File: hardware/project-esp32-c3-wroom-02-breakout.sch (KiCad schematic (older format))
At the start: 10 parts, among them IC1 ESP32-WROVER-E_M213EH6464PH3Q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, J1 Conn_01x06_Male, J2 Conn_01x10_Male, J3 Conn_01x10_Male, Q1 MUN5214DW1T1G, U1 XC6220B331MR

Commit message: Schematic ready
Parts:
- removed C3: 0.1uF, Capacitor_SMD:C_0603_1608Metric_Pad1.08x0.95mm_HandSolder, symbol Device:C_Small
- removed IC1: ESP32-WROVER-E_M213EH6464PH3Q0_, ESP32WROVEREM213EH6464PH3Q0, symbol ESP32-WROVER-E_M213EH6464PH3Q0:ESP32-WROVER-E_M213EH6464PH3Q0_
- removed J1: Conn_01x06_Male, B6B-ZR(LF)(SN):JST_B6B-ZR(LF)(SN), symbol Connector:Conn_01x06_Male
- removed J2, J3: Conn_01x10_Male, Connector_PinHeader_2.54mm:PinHeader_1x10_P2.54mm_Vertical, symbol Connector:Conn_01x10_Male
- removed R1: 10k, Resistor_SMD:R_0603_1608Metric_Pad0.98x0.95mm_HandSolder, symbol Device:R_Small
- added C? (x2): 0.1uF, Capacitor_SMD:C_0603_1608Metric_Pad1.08x0.95mm_HandSolder, symbol Device:C_Small
- added C? (x2): 22pF, Capacitor_SMD:C_0603_1608Metric_Pad1.08x0.95mm_HandSolder, symbol Device:C_Small
- added J?: SM04B-SRSS-TB(LF)(SN), JST_SM04B-SRSS-TB(LF)(SN), symbol SM04B-SRSS-TB_LF__SN_:SM04B-SRSS-TB(LF)(SN)
- added J? (x2): Conn_01x08_Male, symbol Connector:Conn_01x08_Male
- added JP?: SolderJumper_3_Bridged12, symbol Jumper:SolderJumper_3_Bridged12
- added R? (x3): 10k, Resistor_SMD:R_0603_1608Metric_Pad0.98x0.95mm_HandSolder, symbol Device:R_Small
- added R? (x2): 4k7, Resistor_SMD:R_0603_1608Metric_Pad0.98x0.95mm_HandSolder, symbol Device:R_Small
- added U?: ESP32-C3-WROOM-02-H4, MODULE_ESP32-C3-WROOM-02-H4, symbol ESP32-C3-WROOM-02-H4:ESP32-C3-WROOM-02-H4
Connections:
- net labels added: 3V3, GPIO1, GPIO10, GPIO3, GPIO6, GPIO7, GPIO8, GPIO9, SCL, SDA, USB_D+, USB_D-, VCC
- net labels removed: +5V, GPIO14, GPIO15, GPIO18, GPIO19, GPIO21, GPIO22, GPIO23, GPIO25, GPIO26, GPIO27, GPIO32, GPIO33
- wire segments 111 -> 106
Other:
- note added: "Auto Download Boot"
- note added: "Boot Strapping Pins"
- note added: "Connectors"
- note added: "ESP32 Module"
- note added: "I2C/StemmaQT"
- note added: "Regulator"
- note added: "USB"
- note added: "←"
- moved on the sheet: Q1A, Q1B

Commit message: First placement done
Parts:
- added D1: LED, LED_SMD:LED_0603_1608Metric, symbol Device:LED
- added R6: 10k, Resistor_SMD:R_0603_1608Metric_Pad0.98x0.95mm_HandSolder, symbol Device:R_Small
- J2, J3: renamed from J?; footprint (none) -> Connector_PinHeader_2.54mm:PinHeader_1x08_P2.54mm_Vertical
- JP1: renamed from JP?; footprint (none) -> Jumper:SolderJumper-3_P1.3mm_Bridged12_RoundedPad1.0x1.5mm
- gave numbers to parts that had none: 11
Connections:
- wire segments 106 -> 109
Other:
- note added: "Power LED"
- moved on the sheet: J3

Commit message: Routing done
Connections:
- net labels removed: SCL, SDA
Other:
- note added: "(SCL)"
- note added: "(SDA)"
- moved on the sheet: J1, JP1
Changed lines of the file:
@@
 	2800 1400 2800 1300
 Connection ~ 2800 1400
+Text Label 10150 5400 0    50   ~ 0
+RX
 Text Label 10150 5300 0    50   ~ 0
-RX
-Text Label 10150 5400 0    50   ~ 0
 TX
 Text Label 2550 5150 0    50   ~ 0
@@
 Wire Wire Line
 	2550 5850 2850 5850
-Text Label 4300 5350 0    50   ~ 0
-USB_D+
-Text Label 4300 5450 0    50   ~ 0
-USB_D-
-Text Label 4650 5350 0    50   ~ 0
-SDA
-Text Label 4650 5450 0    50   ~ 0
-SCL
-Wire Wire Line
-	4800 5350 4250 5350
-Wire Wire Line
-	4800 5450 4250 5450
 $Comp
 L power:VCC #PWR0108
@@
 Wire Wire Line
 	4900 4400 4900 4350
-Text Label 7450 3100 0    50   ~ 0
-USB_D+
-Text Label 7450 3200 0    50   ~ 0
-USB_D-
-Text Label 9750 3650 0    50   ~ 0
-SDA
-Text Label 9750 3750 0    50   ~ 0
-SCL
 $Comp
 L Device:C_Small C5
@@
 $EndComp
 Wire Wire Line
-	9750 3650 10100 3650
-Wire Wire Line
 	10100 3650 10100 3500
 Wire Wire Line
 	10100 3300 10100 3250
-Wire Wire Line
-	9750 3750 10400 3750
 Wire Wire Line
 	10400 3750 10400 3500
@@
 	9350 5500 9650 5500
 Wire Wire Line
+	10150 5400 10450 5400
+Wire Wire Line
 	10150 5300 10450 5300
-Wire Wire Line
-	10150 5400 10450 5400
 Wire Wire Line
 	10150 5500 10450 5500
@@
 Wire Wire Line
 	9350 5000 9650 5000
-Text Notes 7600 5100 0    197  ~ 0
+Text Notes 7800 5100 0    197  ~ 0
 ←
-Text Notes 8000 5100 0    197  ~ 0
+Text Notes 8200 5100 0    197  ~ 0
 ←
 Wire Wire Line
-	8150 4900 8150 4800
-Wire Wire Line
-	8100 4900 8150 4900
+	8350 4900 8350 4800
+Wire Wire Line
+	8300 4900 8350 4900
 $Comp
 L power:+3.3V #PWR0113
 U 1 1 617D3310
-P 8150 4800
-F 0 "#PWR0113" H 8150 4650 50  0001 C CNN
-F 1 "+3.3V" H 8165 4973 50  0000 C CNN
-F 2 "" H 8150 4800 50  0001 C CNN
-F 3 "" H 8150 4800 50  0001 C CNN
-	1    8150 4800
-	1    0    0    -1
-$EndComp
-Wire Wire Line
-	7650 4900 7700 4900
-Wire Wire Line
-	7650 4800 7650 4900
+P 8350 4800
+F 0 "#PWR0113" H 8350 4650 50  0001 C CNN
+F 1 "+3.3V" H 8365 4973 50  0000 C CNN
+F 2 "" H 8350 4800 50  0001 C CNN
+F 3 "" H 8350 4800 50  0001 C CNN
+	1    8350 4800
+	1    0    0    -1
+$EndComp
+Wire Wire Line
+	7850 4900 7900 4900
+Wire Wire Line
+	7850 4800 7850 4900
 $Comp
 L power:VCC #PWR0114
 U 1 1 617CC8C4
-P 7650 4800
-F 0 "#PWR0114" H 7650 4650 50  0001 C CNN
-F 1 "VCC" H 7665 4973 50  0000 C CNN
-F 2 "" H 7650 4800 50  0001 C CNN
-F 3 "" H 7650 4800 50  0001 C CNN
-	1    7650 4800
-	1    0    0    -1
-$EndComp
-Wire Wire Line
-	7900 5050 7900 5300
+P 7850 4800
+F 0 "#PWR0114" H 7850 4650 50  0001 C CNN
+F 1 "VCC" H 7865 4973 50  0000 C CNN
+F 2 "" H 7850 4800 50  0001 C CNN
+F 3 "" H 7850 4800 50  0001 C CNN
+	1    7850 4800
+	1    0    0    -1
+$EndComp
+Wire Wire Line
+	8100 5050 8100 5300
 $Comp
 L Jumper:SolderJumper_3_Bridged12 JP1
 U 1 1 617A1A5E
-P 7900 4900
-F 0 "JP1" H 7900 5013 50  0000 C CNN
-F 1 "SolderJumper_3_Bridged12" H 7900 5014 50  0001 C CNN
-F 2 "Jumper:SolderJumper-3_P1.3mm_Bridged12_RoundedPad1.0x1.5mm" H 7900 4900 50  0001 C CNN
-F 3 "~" H 7900 4900 50  0001 C CNN
-	1    7900 4900
-	1    0    0    -1
-$EndComp
-Wire Wire Line
-	7700 5700 7700 5200
-Connection ~ 7700 5700
-Wire Wire Line
-	8000 5700 7700 5700
-Wire Wire Line
-	7800 5500 8000 5500
-Wire Wire Line
-	8000 5400 7800 5400
-Text Label 7800 5400 0    50   ~ 0
-SDA
-Text Label 7800 5500 0    50   ~ 0
-SCL
+P 8100 4900
+F 0 "JP1" H 8100 5013 50  0000 C CNN
+F 1 "SolderJumper_3_Bridged12" H 8100 5014 50  0001 C CNN
+F 2 "Jumper:SolderJumper-3_P1.3mm_Bridged12_RoundedPad1.0x1.5mm" H 8100 4900 50  0001 C CNN
+F 3 "~" H 8100 4900 50  0001 C CNN
+	1    8100 4900
+	1    0    0    -1
+$EndComp
+Wire Wire Line
+	8200 5700 7550 5700
 $Comp
 L power:GND #PWR0115
 U 1 1 616AF751
-P 7700 5800
-F 0 "#PWR0115" H 7700 5550 50  0001 C CNN
-F 1 "GND" H 7705 5627 50  0000 C CNN
-F 2 "" H 7700 5800 50  0001 C CNN
-F 3 "" H 7700 5800 50  0001 C CNN
-	1    7700 5800
-	1    0    0    -1
-$EndComp
-Wire Wire Line
-	7700 5800 7700 5700
-Wire Wire Line
-	7700 5200 8000 5200
-Wire Wire Line
-	7900 5300 8000 5300
+P 7550 5800
+F 0 "#PWR0115" H 7550 5550 50  0001 C CNN
+F 1 "GND" H 7555 5627 50  0000 C CNN
+F 2 "" H 7550 5800 50  0001 C CNN
+F 3 "" H 7550 5800 50  0001 C CNN
+	1    7550 5800
+	1    0    0    -1
+$EndComp
+Wire Wire Line
+	7550 5800 7550 5700
+Wire Wire Line
+	8100 5300 8200 5300
 $Comp
 L SM04B-SRSS-TB_LF__SN_:SM04B-SRSS-TB(LF)(SN) J1
 U 1 1 6168E703
-P 8300 5400
-F 0 "J1" H 8530 5350 50  0000 L CNN
-F 1 "SM04B-SRSS-TB(LF)(SN)" H 8530 5305 50  0001 L CNN
-F 2 "JST_SM04B-SRSS-TB(LF)(SN)" H 8300 5400 50  0001 L BNN
-F 3 "" H 8300 5400 50  0001 L BNN
-F 4 "Manufacturer recommendations" H 8300 5400 50  0001 L BNN "STANDARD"
-F 5 "JST" H 8300 5400 50  0001 L BNN "MANUFACTURER"
-	1    8300 5400
+P 8500 5400
+F 0 "J1" H 8730 5350 50  0000 L CNN
+F 1 "SM04B-SRSS-TB(LF)(SN)" H 8730 5305 50  0001 L CNN
+F 2 "JST_SM04B-SRSS-TB(LF)(SN)" H 8500 5400 50  0001 L BNN
+F 3 "" H 8500 5400 50  0001 L BNN
+F 4 "Manufacturer recommendations" H 8500 5400 50  0001 L BNN "STANDARD"
+F 5 "JST" H 8500 5400 50  0001 L BNN "MANUFACTURER"
+	1    8500 5400
 	1    0    0    -1
 $EndComp
@@
 Text Notes 8850 650  0    50   ~ 0
 Power LED
+Text Label 9550 3750 0    50   ~ 0
+USB_D+
+Text Label 9550 3650 0    50   ~ 0
+USB_D-
+Wire Wire Line
+	9550 3650 10100 3650
+Wire Wire Line
+	9550 3750 10400 3750
+Text Label 7450 3200 0    50   ~ 0
+USB_D+
+Text Label 7450 3100 0    50   ~ 0
+USB_D-
+Text Label 7900 5400 0    50   ~ 0
+USB_D+
+Text Label 7900 5500 0    50   ~ 0
+USB_D-
+Wire Wire Line
+	7550 5200 7550 5700
+Wire Wire Line
+	7550 5200 8200 5200
+Connection ~ 7550 5700
+Text Label 4300 5450 0    50   ~ 0
+USB_D+
+Wire Wire Line
+	4550 5350 4250 5350
+Wire Wire Line
+	4550 5450 4250 5450
+Text Notes 9300 3750 0    50   ~ 0
+(SDA)
+Text Notes 9300 3650 0    50   ~ 0
+(SCL)
+Text Notes 7650 5400 0    50   ~ 0
+(SDA)
+Text Notes 7650 5500 0    50   ~ 0
+(SCL)
+Wire Wire Line
+	7900 5400 8200 5400
+Wire Wire Line
+	7900 5500 8200 5500
+Text Label 4300 5350 0    50   ~ 0
+USB_D-
+Text Notes 4650 5450 0    50   ~ 0
+(SDA)
+Text Notes 4650 5350 0    50   ~ 0
+(SCL)
 $EndSCHEMATC

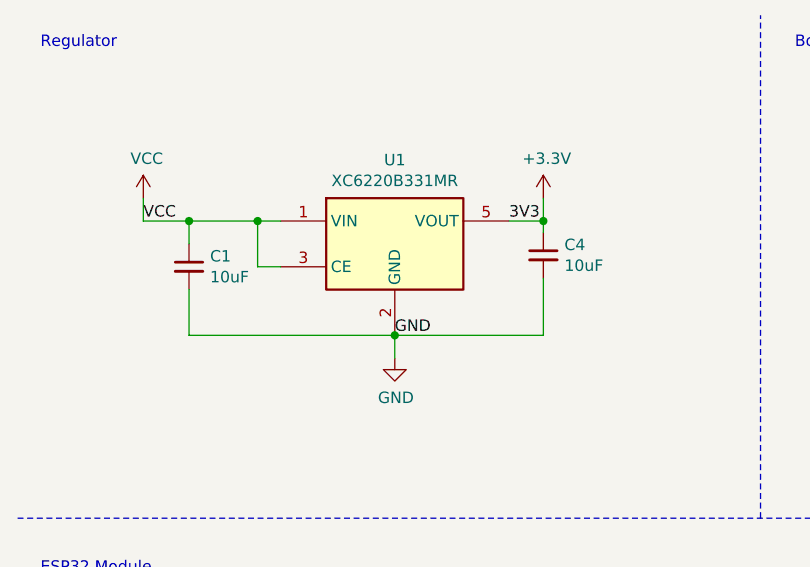
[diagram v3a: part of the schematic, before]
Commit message: Fix reg cap values in schematic
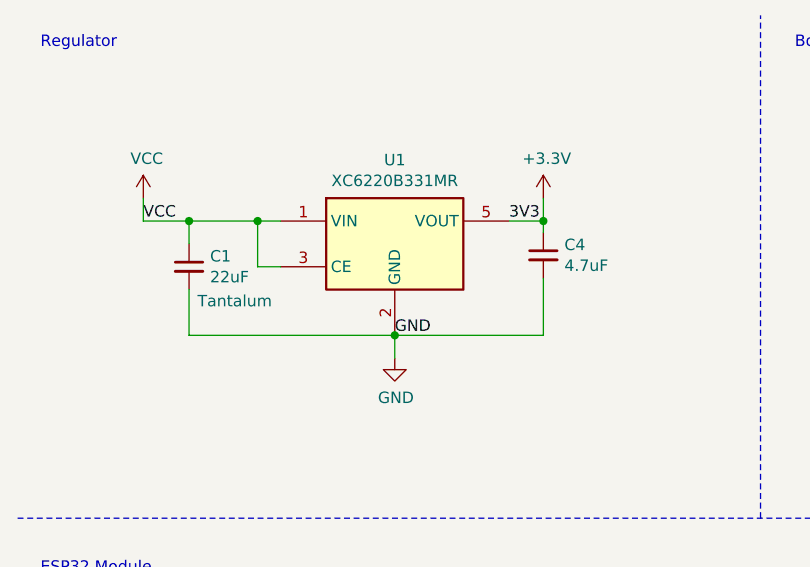
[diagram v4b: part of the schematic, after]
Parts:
- C1: value 10uF -> 22uF; Type (none) -> Tantalum
- C4: value 10uF -> 4.7uF
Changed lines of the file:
@@
 P 1250 1600
 F 0 "C1" H 1342 1646 50  0000 L CNN
-F 1 "10uF" H 1342 1555 50  0000 L CNN
+F 1 "22uF" H 1342 1555 50  0000 L CNN
 F 2 "Capacitor_SMD:C_0805_2012Metric_Pad1.18x1.45mm_HandSolder" H 1250 1600 50  0001 C CNN
 F 3 "~" H 1250 1600 50  0001 C CNN
+F 4 "Tantalum" H 1450 1450 50  0000 C CNN "Type"
 	1    1250 1600
 	1    0    0    -1
@@
 P 2800 1550
 F 0 "C4" H 2892 1596 50  0000 L CNN
-F 1 "10uF" H 2892 1505 50  0000 L CNN
+F 1 "4.7uF" H 2892 1505 50  0000 L CNN
 F 2 "Capacitor_SMD:C_0805_2012Metric_Pad1.18x1.45mm_HandSolder" H 2800 1550 50  0001 C CNN
 F 3 "~" H 2800 1550 50  0001 C CNN

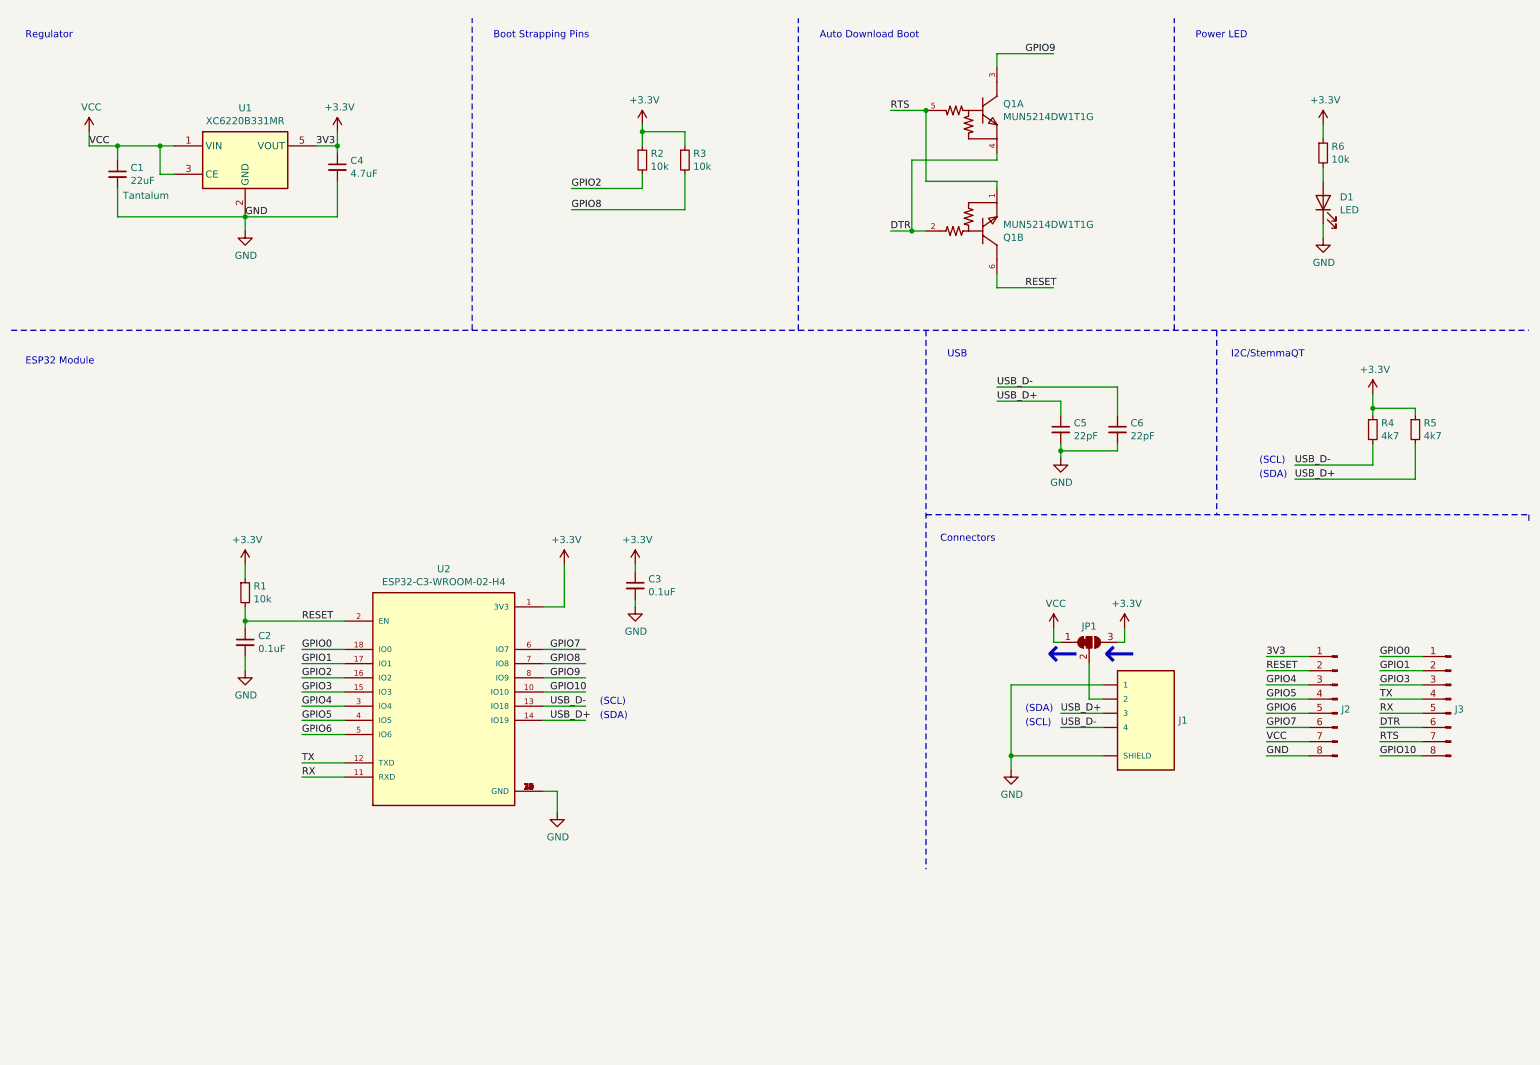
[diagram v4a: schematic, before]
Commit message: Add USB port to schematic
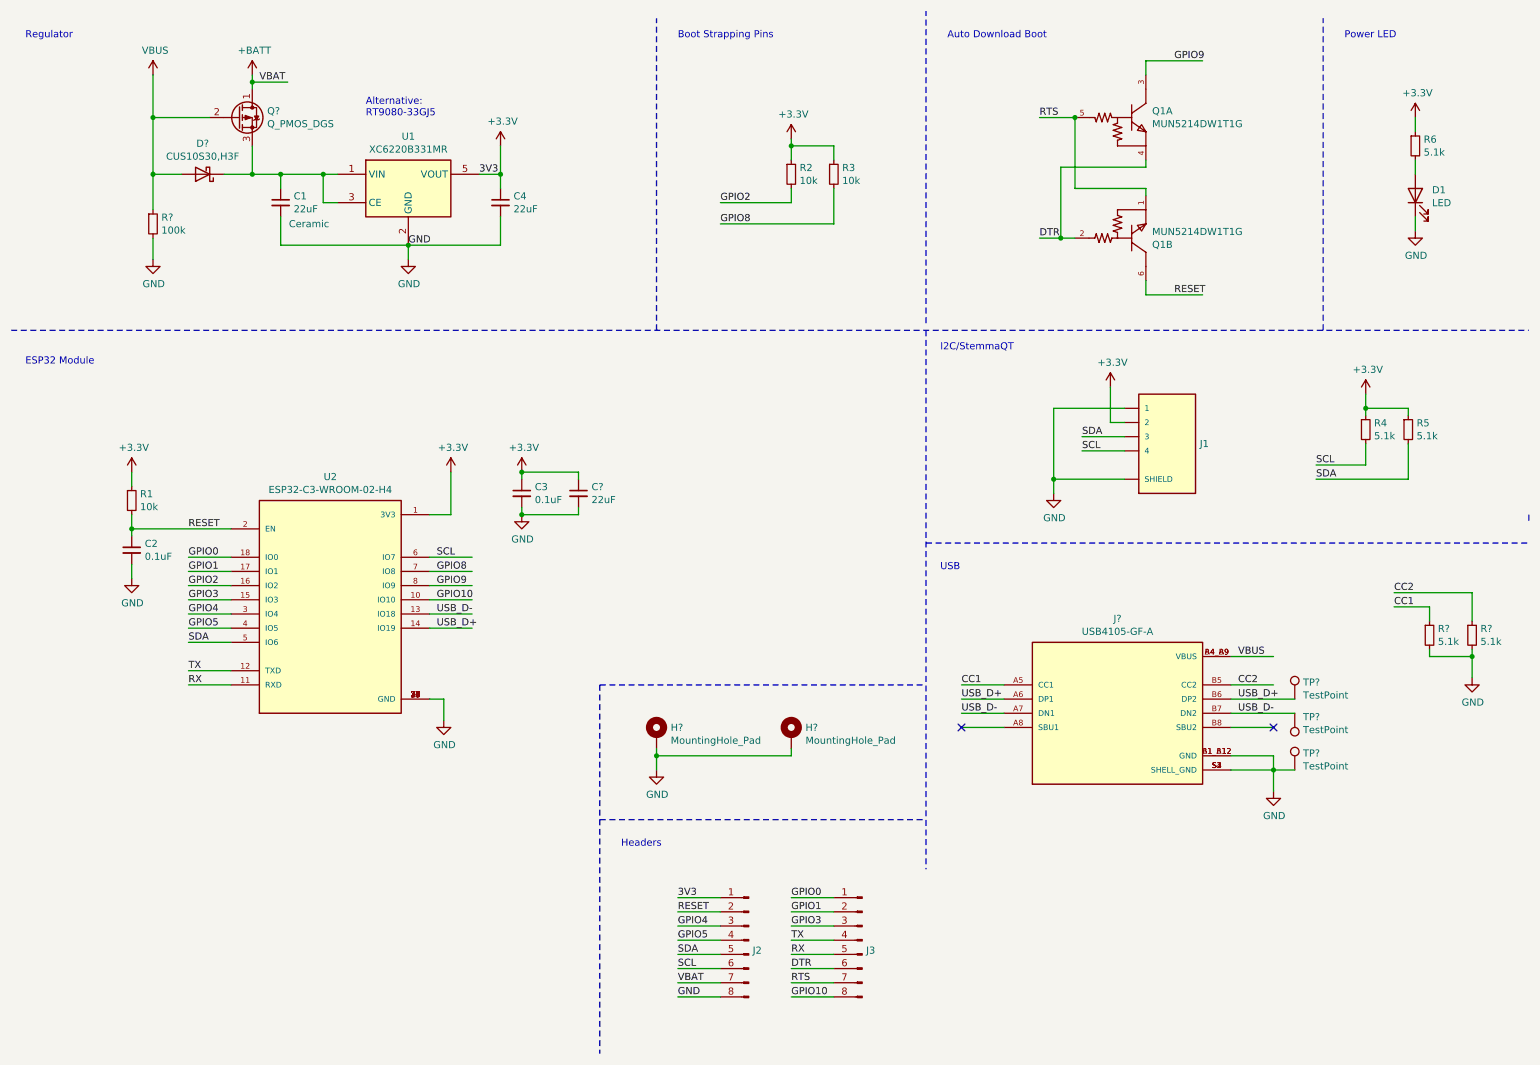
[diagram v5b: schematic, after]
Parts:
- removed C5, C6: 22pF, Capacitor_SMD:C_0603_1608Metric_Pad1.08x0.95mm_HandSolder, symbol Device:C_Small
- removed JP1: SolderJumper_3_Bridged12, Jumper:SolderJumper-3_P1.3mm_Bridged12_RoundedPad1.0x1.5mm, symbol Jumper:SolderJumper_3_Bridged12
- added C?: 22uF, Capacitor_SMD:C_0805_2012Metric_Pad1.18x1.45mm_HandSolder, symbol Device:C_Small
- added D?: CUS10S30,H3F‎, CUS10S30,H3F:DIO_CUS520,H3F, symbol Device:D_Schottky
- added H? (x2): MountingHole_Pad, MountingHole:MountingHole_2.7mm_M2.5_ISO7380_Pad, symbol Mechanical:MountingHole_Pad
- added J?: USB4105-GF-A, GCT_USB4105-GF-A, symbol USB4105-GF-A:USB4105-GF-A
- added Q?: Q_PMOS_DGS, SSM6J214FE-TE85L-F:SOT50P160X60-6N, symbol Device:Q_PMOS_DGS
- added R? (x2): 5.1k, Resistor_SMD:R_0603_1608Metric_Pad0.98x0.95mm_HandSolder, symbol Device:R_Small
- added R?: 100k, Resistor_SMD:R_0603_1608Metric_Pad0.98x0.95mm_HandSolder, symbol Device:R_Small
- added TP? (x3): TestPoint, TestPoint:TestPoint_Pad_D1.0mm, symbol Connector:TestPoint
- C1: Type Tantalum -> Ceramic
- C4: value 4.7uF -> 22uF
- R4, R5: value 4k7 -> 5.1k
- R6: value 10k -> 5.1k
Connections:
- net labels added: +BATT, CC1, CC2, SCL, SDA, VBAT, VBUS
- net labels removed: GPIO6, GPIO7, VCC
- wire segments 109 -> 137
- no-connect marks 0 -> 2
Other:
- note added: "Alternative:\n‎RT9080-33GJ5‎"
- note added: "Headers"
- note removed: "(SCL)"
- note removed: "(SDA)"
- note removed: "Connectors"
- note removed: "←"
- moved on the sheet: C1, C2, C3, C4, D1, J1, J2, J3, Q1A, Q1B, R1, R2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
